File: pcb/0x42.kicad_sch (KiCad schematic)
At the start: 32 parts, among them J1 USB_C_Receptacle_USB2.0, J2 Conn_01x04, J3 SWD_CN4, SW1 Reset, SW2 Boot, U1 STM32F072CBUx, U2 MCP1700-3302E_SOT89

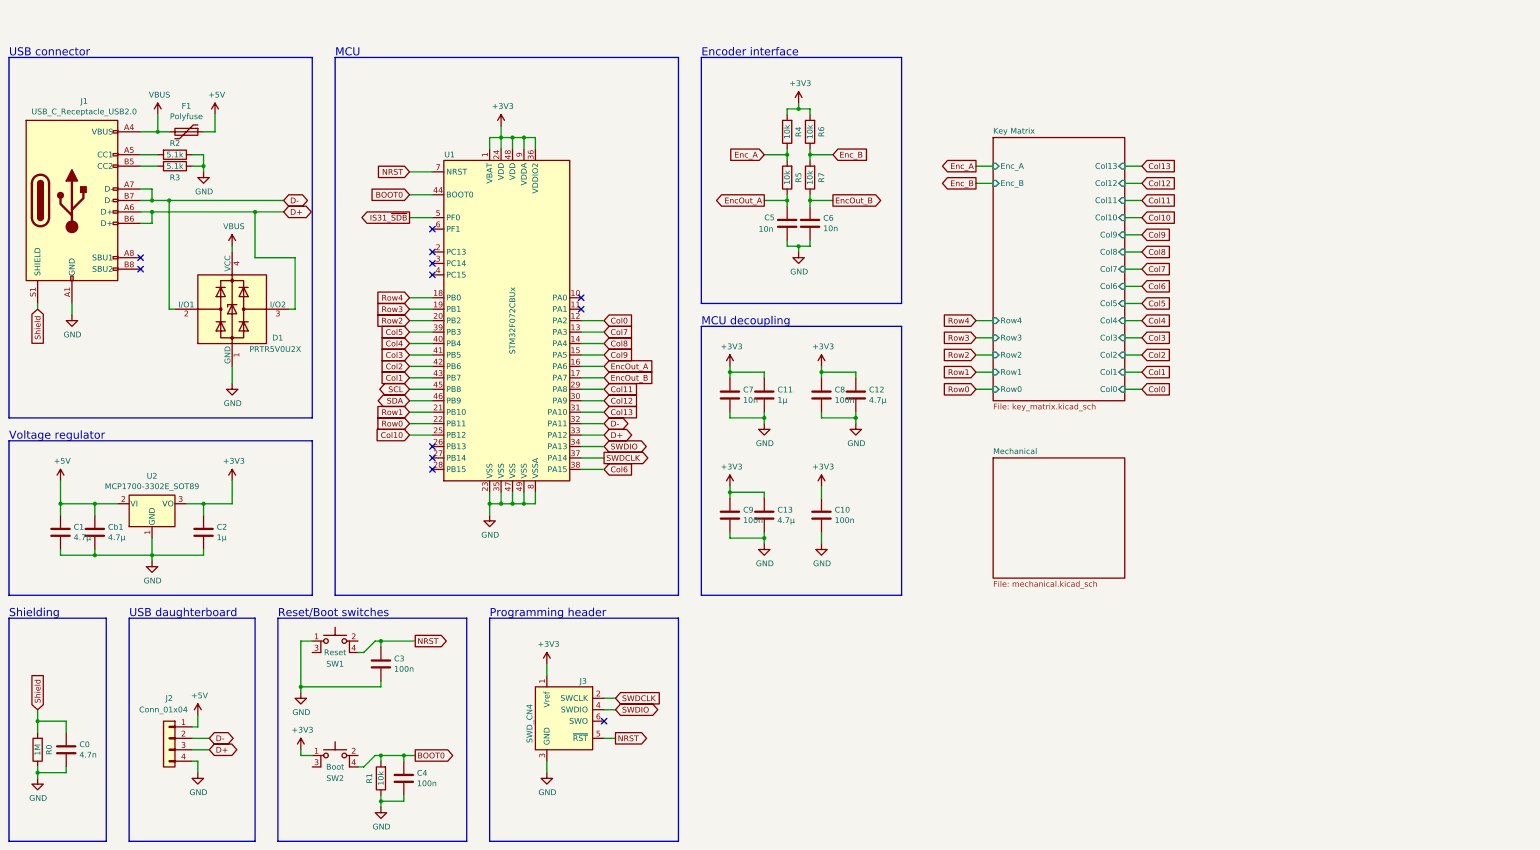
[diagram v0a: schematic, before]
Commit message: Switched to RP2040 - PCB finalization
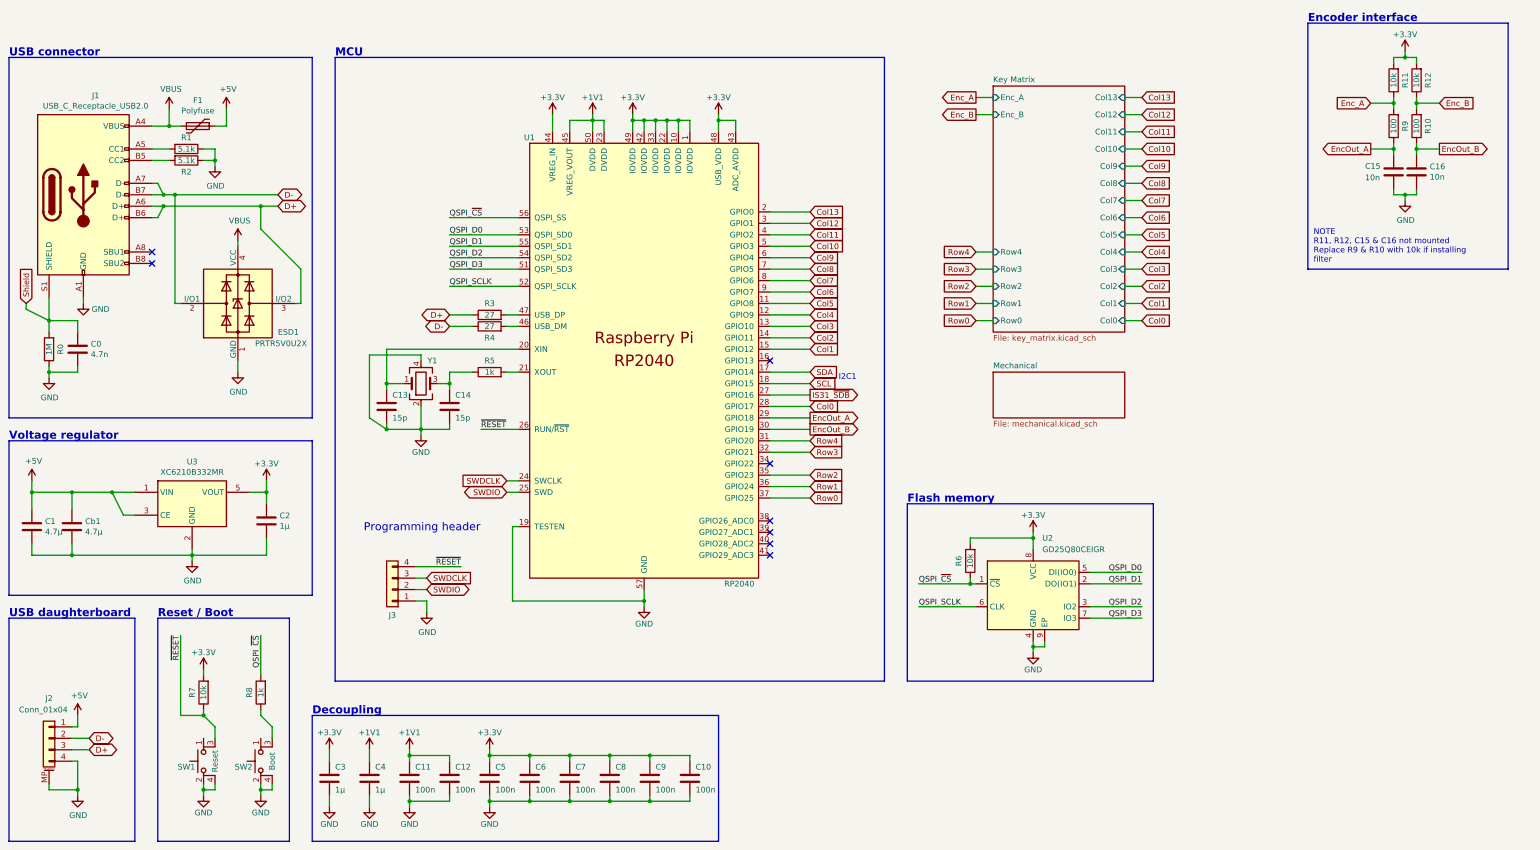
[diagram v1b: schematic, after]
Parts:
- removed J3: SWD_CN4, 0xLib_STM32:SWD_1x06_P2.54mm_POGO, symbol 0xLib_STM32:SWD_CN4
- removed R1: 10k, 0xLib_Passive_SMD:R_0603_1608Metric, symbol Device:R
- removed U1: STM32F072CBUx, Package_DFN_QFN:QFN-48-1EP_7x7mm_P0.5mm_EP5.6x5.6mm, symbol MCU_ST_STM32F0:STM32F072CBUx
- removed U2: MCP1700-3302E_SOT89, Package_TO_SOT_SMD:SOT-89-3, symbol Regulator_Linear:MCP1700-3302E_SOT89
- added C14: 15p, 0xLib_Passive_SMD:C_0603_1608Metric, symbol Device:C
- added C5, C6: 100n, 0xLib_Passive_SMD:C_0603_1608Metric, symbol Device:C
- added J3: Conn_01x03, Connector_PinHeader_2.54mm:PinHeader_1x04_P2.54mm_Vertical, symbol Connector_Generic:Conn_01x04
- added R3, R4: 27, 0xLib_Passive_SMD:R_0603_1608Metric, symbol Device:R
- added R5, R8: 1k, 0xLib_Passive_SMD:R_0603_1608Metric, symbol Device:R
- added R6, R7: 10k, 0xLib_Passive_SMD:R_0603_1608Metric, symbol Device:R
- added U1: RP2040, 0xLib_Package_DFN_QFN:QFN-56-1EP_7x7mm_P0.4mm_EP3.2x3.2mm, symbol 0xLib_MCU_RaspberryPi_RP2040:RP2040
- added U2: GD25Q80CEIGR, 0xLib_Package_DFN_QFN:USON-8-1EP_3x2mm_P0.5mm_EP0.25x1.65mm, symbol Memory_Flash:W25Q32JVZP
- added U3: XC6210B332MR, 0xLib_TO_SOT_SMD:SOT-23-5, symbol Regulator_Linear:XC6210B332MR
- added Y1: Crystal_GND24, Crystal:Crystal_SMD_2520-4Pin_2.5x2.0mm, symbol Device:Crystal_GND24
- C0: LCSC (none) -> C1744
- C1: LCSC (none) -> C1779
- C10, C8, C9: LCSC (none) -> C14663
- C11: value 1µ -> 100n; LCSC (none) -> C14663
- C12: value 4.7µ -> 100n; LCSC (none) -> C14663
- C13: value 4.7µ -> 15p; LCSC (none) -> C1644
- C15: renamed from C5; LCSC (none) -> C57112; now left out of the parts list
- C16: renamed from C6; LCSC (none) -> C57112; now left out of the parts list
- C2: LCSC (none) -> C15849
- C3, C4: value 100n -> 1µ; LCSC (none) -> C15849
- C7: value 10n -> 100n; LCSC (none) -> C14663
- Cb1: LCSC (none) -> C1779; now left out of the parts list
- ESD1: renamed from D1; LCSC (none) -> C2827688
- F1: LCSC (none) -> C315893
- J1: LCSC (none) -> C165948
- J2: symbol Connector_Generic:Conn_01x04 -> Connector_Generic_MountingPin:Conn_01x04_MountingPin; LCSC (none) -> C160404
- R0: LCSC (none) -> C22935
- R1: renamed from R2; LCSC (none) -> C23186
- R10: renamed from R7; value 10k -> 100; LCSC (none) -> C22775
- R11: renamed from R4; LCSC (none) -> C25804; now left out of the parts list
- R12: renamed from R6; LCSC (none) -> C25804; now left out of the parts list
- R2: renamed from R3; LCSC (none) -> C23186
- R9: renamed from R5; value 10k -> 100; LCSC (none) -> C22775
- SW1, SW2: LCSC (none) -> C318884
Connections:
- net +5V: now also U3.1 (VIN), U3.3 (CE)
- net Col0: now also U1.28 (GPIO17)
- net Col1: now also U1.15 (GPIO12)
- net Col10: now also U1.5 (GPIO3)
- net Col11: now also U1.4 (GPIO2)
- net Col12: now also U1.3 (GPIO1)
- net Col13: now also U1.2 (GPIO0)
- net Col2: now also U1.14 (GPIO11)
- net Col3: now also U1.13 (GPIO10)
- net Col4: now also U1.12 (GPIO9)
- net Col5: now also U1.11 (GPIO8)
- net Col6: now also U1.9 (GPIO7)
- net Col7: now also U1.8 (GPIO6)
- net Col8: now also U1.7 (GPIO5)
- net Col9: now also U1.6 (GPIO4)
- net D+: now also R3.1
- net D-: now also R4.1
- net EncOut_A: now also U1.29 (GPIO18)
- net EncOut_B: now also U1.30 (GPIO19)
- net GND: now also J2.MP (MountPin), SW1.2, SW1.4, SW2.2, SW2.4, C14.2, C5.2, C6.2, J3.1 (Pin_1), U1.19 (TESTEN), U1.57 (GND), U2.4 (GND), U2.9 (EP), U3.2 (GND), Y1.2, Y1.4; no longer SW1.1
- net IS31_~{SDB}: now also U1.27 (GPIO16)
- net Row0: now also U1.37 (GPIO25)
- net Row1: now also U1.36 (GPIO24)
- net Row2: now also U1.35 (GPIO23)
- net Row3: now also U1.32 (GPIO21)
- net Row4: now also U1.31 (GPIO20)
- net SCL: now also U1.18 (GPIO15)
- net SDA: now also U1.17 (GPIO14)
- net SWDCLK: now also J3.3 (Pin_3), U1.24 (SWCLK)
- net SWDIO: now also J3.2 (Pin_2), U1.25 (SWD)
- net at SW2.3: now also R8.1
- net ~{RESET}: now reaches SW1.3
- net ~{RESET}: now also J3.4 (Pin_4), R7.1, U1.26 (RUN/~{RST})
- net +3V3 renamed +3.3V
- net +3.3V: now also C3.1, C5.1, C6.1, R6.2, R7.2, U1.1 (IOVDD), U1.10 (IOVDD), U1.22 (IOVDD), U1.33 (IOVDD), U1.42 (IOVDD), U1.43 (ADC_AVDD), U1.44 (VREG_IN), U1.48 (USB_VDD), U1.49 (IOVDD), U2.8 (VCC), U3.5 (VOUT); no longer C11.1, C12.1, C13.1, SW2.1
- net BOOT0 renamed +1V1
- net +1V1: now also C11.1, C12.1, U1.23 (DVDD), U1.45 (VREG_VOUT), U1.50 (DVDD); no longer SW2.4
- removed net NRST: C3.1, SW1.4
- new net: C13.1, U1.20 (XIN), Y1.1
- new net: C14.1, R5.1, Y1.3
- new net: R5.2, U1.21 (XOUT)
- new net: R4.2, U1.46 (USB_DM)
- new net: R3.2, U1.47 (USB_DP)
- new net QSPI_D0: U1.53 (QSPI_SD0), U2.5 (DI(IO0))
- new net QSPI_D1: U1.55 (QSPI_SD1), U2.2 (DO(IO1))
- new net QSPI_D2: U1.54 (QSPI_SD2), U2.3 (IO2)
- new net QSPI_D3: U1.51 (QSPI_SD3), U2.7 (IO3)
- new net QSPI_SCLK: U1.52 (QSPI_SCLK), U2.6 (CLK)
- new net QSPI_~{CS}: R6.1, R8.2, U1.56 (QSPI_SS), U2.1 (~{CS})
- no-connect marks 12 -> 8
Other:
- note added: "Decoupling"
- note added: "Flash memory"
- note added: "I2C1"
- note added: "NOTE R11, R12, C15 & C16 not mounted Replace R9 & R10 with 10k if installing filter"
- note added: "Reset / Boot"
- note removed: "MCU decoupling"
- note removed: "Reset/Boot switches"
- note removed: "Shielding"
- moved on the sheet: C0, C1, C15, C16, C2, Cb1, ESD1, F1, J1, R0, R1, R10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
